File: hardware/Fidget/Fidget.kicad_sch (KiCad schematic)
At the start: 41 parts

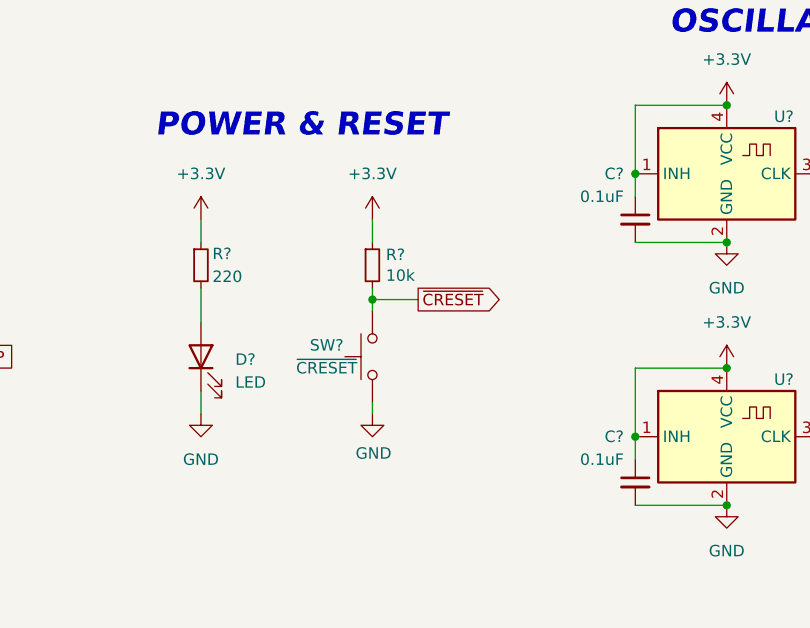
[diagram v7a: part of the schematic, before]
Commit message: Got simple RTL experiment of USART<->Bus in TinyFPGA
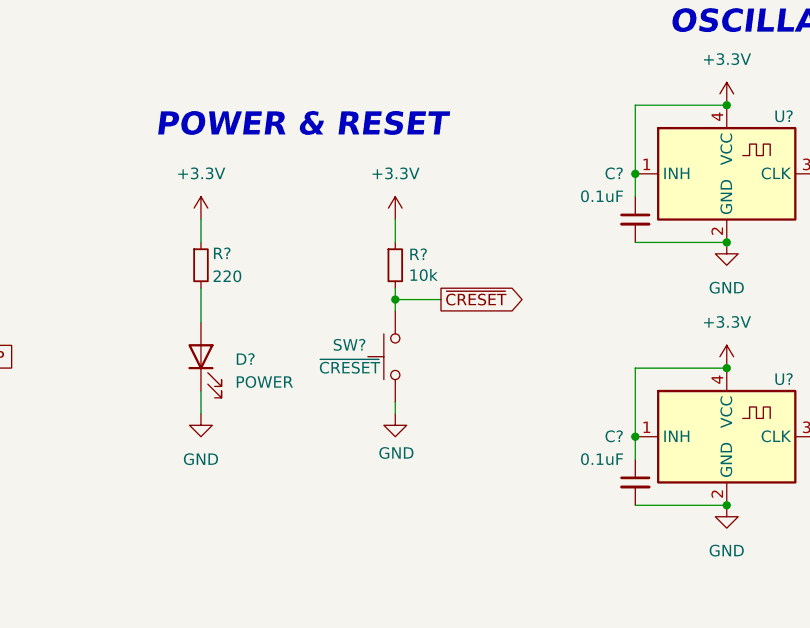
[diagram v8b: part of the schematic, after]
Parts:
- D?: value LED -> POWER
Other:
- moved on the sheet: R?, SW?
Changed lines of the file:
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@@
   (junction (at 245.11 110.49) (diameter 0) (color 0 0 0 0)
   )
-  (junction (at 205.74 132.08) (diameter 0) (color 0 0 0 0)
+  (junction (at 208.28 132.08) (diameter 0) (color 0 0 0 0)
   )
   (junction (at 110.49 130.81) (diameter 0) (color 0 0 0 0)
@@
     (stroke (width 0) (type default) (color 0 0 0 0))
   )
-  (wire (pts (xy 210.82 132.08) (xy 205.74 132.08))
-    (stroke (width 0) (type default) (color 0 0 0 0))
-  )
-  (wire (pts (xy 205.74 132.08) (xy 205.74 130.81))
+  (wire (pts (xy 213.36 132.08) (xy 208.28 132.08))
+    (stroke (width 0) (type default) (color 0 0 0 0))
+  )
+  (wire (pts (xy 208.28 132.08) (xy 208.28 130.81))
     (stroke (width 0) (type default) (color 0 0 0 0))
   )
@@
     (stroke (width 0) (type default) (color 0 0 0 0))
   )
-  (wire (pts (xy 205.74 123.19) (xy 205.74 125.73))
+  (wire (pts (xy 208.28 123.19) (xy 208.28 125.73))
     (stroke (width 0) (type default) (color 0 0 0 0))
   )
@@
     (stroke (width 0) (type default) (color 0 0 0 0))
   )
-  (wire (pts (xy 205.74 132.08) (xy 205.74 133.35))
+  (wire (pts (xy 208.28 132.08) (xy 208.28 133.35))
     (stroke (width 0) (type default) (color 0 0 0 0))
   )
@@
     (stroke (width 0) (type default) (color 0 0 0 0))
   )
-  (wire (pts (xy 205.74 143.51) (xy 205.74 144.78))
+  (wire (pts (xy 208.28 143.51) (xy 208.28 144.78))
     (stroke (width 0) (type default) (color 0 0 0 0))
   )
@@
     )
   )
-  (global_label "~{CRESET}" (shape output) (at 210.82 132.08 0) (fields_autoplaced)
+  (global_label "~{CRESET}" (shape output) (at 213.36 132.08 0) (fields_autoplaced)
     (effects (font (size 1.27 1.27)) (justify left))
-    (property "Intersheet References" "${INTERSHEET_REFS}" (id 0) (at 220.2483 132.0006 0)
+    (property "Intersheet References" "${INTERSHEET_REFS}" (id 0) (at 222.7883 132.0006 0)
       (effects (font (size 1.27 1.27)) (justify left) hide)
     )
@@
     (pin "1")
   )
-  (symbol (lib_id "Device:R_Small") (at 205.74 128.27 0) (unit 1)
-    (in_bom yes) (on_board yes)
-    (property "Reference" "R?" (id 0) (at 207.2386 127.1016 0)
-      (effects (font (size 1.27 1.27)) (justify left))
-    )
-    (property "Value" "10k" (id 1) (at 207.2386 129.413 0)
-      (effects (font (size 1.27 1.27)) (justify left))
-    )
-    (property "Footprint" "Resistor_THT:R_Axial_DIN0204_L3.6mm_D1.6mm_P5.08mm_Horizontal" (id 2) (at 205.74 128.27 0)
-      (effects (font (size 1.27 1.27)) hide)
-    )
-    (property "Datasheet" "~" (id 3) (at 205.74 128.27 0)
+  (symbol (lib_id "Device:R_Small") (at 208.28 128.27 0) (unit 1)
+    (in_bom yes) (on_board yes)
+    (property "Reference" "R?" (id 0) (at 209.7786 127.1016 0)
+      (effects (font (size 1.27 1.27)) (justify left))
+    )
+    (property "Value" "10k" (id 1) (at 209.7786 129.413 0)
+      (effects (font (size 1.27 1.27)) (justify left))
+    )
+    (property "Footprint" "Resistor_THT:R_Axial_DIN0204_L3.6mm_D1.6mm_P5.08mm_Horizontal" (id 2) (at 208.28 128.27 0)
+      (effects (font (size 1.27 1.27)) hide)
+    )
+    (property "Datasheet" "~" (id 3) (at 208.28 128.27 0)
       (effects (font (size 1.27 1.27)) hide)
     )
@@
     (pin "1")
   )
-  (symbol (lib_id "power:+3.3V") (at 205.74 123.19 0) (unit 1)
-    (in_bom yes) (on_board yes) (fields_autoplaced)
-    (property "Reference" "#PWR0149" (id 0) (at 205.74 127 0)
-      (effects (font (size 1.27 1.27)) hide)
-    )
-    (property "Value" "+3.3V" (id 1) (at 205.74 118.11 0))
-    (property "Footprint" "" (id 2) (at 205.74 123.19 0)
-      (effects (font (size 1.27 1.27)) hide)
-    )
-    (property "Datasheet" "" (id 3) (at 205.74 123.19 0)
+  (symbol (lib_id "power:+3.3V") (at 208.28 123.19 0) (unit 1)
+    (in_bom yes) (on_board yes) (fields_autoplaced)
+    (property "Reference" "#PWR0149" (id 0) (at 208.28 127 0)
+      (effects (font (size 1.27 1.27)) hide)
+    )
+    (property "Value" "+3.3V" (id 1) (at 208.28 118.11 0))
+    (property "Footprint" "" (id 2) (at 208.28 123.19 0)
+      (effects (font (size 1.27 1.27)) hide)
+    )
+    (property "Datasheet" "" (id 3) (at 208.28 123.19 0)
       (effects (font (size 1.27 1.27)) hide)
     )
@@
     (pin "2")
   )
-  (symbol (lib_id "power:GND") (at 205.74 144.78 0) (unit 1)
-    (in_bom yes) (on_board yes)
-    (property "Reference" "#PWR0150" (id 0) (at 205.74 151.13 0)
-      (effects (font (size 1.27 1.27)) hide)
-    )
-    (property "Value" "GND" (id 1) (at 205.867 149.1742 0))
-    (property "Footprint" "" (id 2) (at 205.74 144.78 0)
-      (effects (font (size 1.27 1.27)) hide)
-    )
-    (property "Datasheet" "" (id 3) (at 205.74 144.78 0)
+  (symbol (lib_id "power:GND") (at 208.28 144.78 0) (unit 1)
+    (in_bom yes) (on_board yes)
+    (property "Reference" "#PWR0150" (id 0) (at 208.28 151.13 0)
+      (effects (font (size 1.27 1.27)) hide)
+    )
+    (property "Value" "GND" (id 1) (at 208.407 149.1742 0))
+    (property "Footprint" "" (id 2) (at 208.28 144.78 0)
+      (effects (font (size 1.27 1.27)) hide)
+    )
+    (property "Datasheet" "" (id 3) (at 208.28 144.78 0)
       (effects (font (size 1.27 1.27)) hide)
     )
@@
     (pin "2")
   )
-  (symbol (lib_id "Switch:SW_Push") (at 205.74 138.43 90) (unit 1)
-    (in_bom yes) (on_board yes)
-    (property "Reference" "SW?" (id 0) (at 200.66 137.16 90))
-    (property "Value" "~{CRESET}" (id 1) (at 200.66 139.7 90))
-    (property "Footprint" "Button_Switch_THT:SW_PUSH_6mm" (id 2) (at 200.66 138.43 0)
-      (effects (font (size 1.27 1.27)) hide)
-    )
-    (property "Datasheet" "~" (id 3) (at 200.66 138.43 0)
+  (symbol (lib_id "Switch:SW_Push") (at 208.28 138.43 90) (unit 1)
+    (in_bom yes) (on_board yes)
+    (property "Reference" "SW?" (id 0) (at 203.2 137.16 90))
+    (property "Value" "~{CRESET}" (id 1) (at 203.2 139.7 90))
+    (property "Footprint" "Button_Switch_THT:SW_PUSH_6mm" (id 2) (at 203.2 138.43 0)
+      (effects (font (size 1.27 1.27)) hide)
+    )
+    (property "Datasheet" "~" (id 3) (at 203.2 138.43 0)
       (effects (font (size 1.27 1.27)) hide)
     )
@@
       (effects (font (size 1.27 1.27)) (justify right))
     )
-    (property "Value" "LED" (id 1) (at 190.5 141.2874 90)
+    (property "Value" "POWER" (id 1) (at 190.5 141.2874 90)
       (effects (font (size 1.27 1.27)) (justify right))
     )
@@
       (reference "#PWR0201") (unit 1) (value "+3.3V") (footprint "")
     )
+    (path "/78dabe45-a56e-4c1c-abf8-a53679340cd9/32af5117-4867-459b-9fc5-3930d31b079c"
+      (reference "#PWR?") (unit 1) (value "GND") (footprint "")
+    )
+    (path "/78dabe45-a56e-4c1c-abf8-a53679340cd9/4a6908bb-cf20-4883-990b-62288f60f364"
+      (reference "#PWR?") (unit 1) (value "GND") (footprint "")
+    )
+    (path "/78dabe45-a56e-4c1c-abf8-a53679340cd9/5ad1548b-6500-4e21-9929-dc51aff281a5"
+      (reference "#PWR?") (unit 1) (value "+3.3V") (footprint "")
+    )
+    (path "/78dabe45-a56e-4c1c-abf8-a53679340cd9/646e8379-3038-4153-ab95-dc981463368d"
+      (reference "#PWR?") (unit 1) (value "GND") (footprint "")
+    )
+    (path "/78dabe45-a56e-4c1c-abf8-a53679340cd9/712d8644-5eb7-4bcc-bfe9-8b7f5c84fca8"
+      (reference "#PWR?") (unit 1) (value "+3.3V") (footprint "")
+    )
+    (path "/78dabe45-a56e-4c1c-abf8-a53679340cd9/b5d5925b-ed9f-4e3a-b427-99111acc3c01"
+      (reference "#PWR?") (unit 1) (value "GND") (footprint "")
+    )
     (path "/636ee855-2082-46e2-a822-b2da99283a14/0104126c-d7db-4e9c-879f-fe393c49bd40"
       (reference "C?") (unit 1) (value "0.1uF") (footprint "")
@@
       (reference "C?") (unit 1) (value "0.1uF") (footprint "")
     )
+    (path "/78dabe45-a56e-4c1c-abf8-a53679340cd9/2ee9b547-73b8-4502-8eb1-38d06f282605"
+      (reference "D?") (unit 1) (value "UL1") (footprint "")
+    )
+    (path "/78dabe45-a56e-4c1c-abf8-a53679340cd9/929e1288-08e9-45d3-95e0-6f0f74cf978f"
+      (reference "D?") (unit 1) (value "UL2") (footprint "")
+    )
     (path "/fc064560-d1a5-4c2f-a4ad-ae42d5f9cadb"
-      (reference "D?") (unit 1) (value "LED") (footprint "")
+      (reference "D?") (unit 1) (value "POWER") (footprint "")
     )
     (path "/02f7746c-715c-4734-bcc3-9f6f4cf1447e"
@@
       (reference "R?") (unit 1) (value "68") (footprint "")
     )
+    (path "/78dabe45-a56e-4c1c-abf8-a53679340cd9/19d67f88-a082-4c8d-8f95-07e071cfad85"
+      (reference "R?") (unit 1) (value "10k") (footprint "Resistor_THT:R_Axial_DIN0204_L3.6mm_D1.6mm_P5.08mm_Horizontal")
+    )
+    (path "/78dabe45-a56e-4c1c-abf8-a53679340cd9/1f10bb6d-c48a-4e92-82ff-956ea432e3c4"
+      (reference "R?") (unit 1) (value "220") (footprint "")
+    )
     (path "/246cd007-a62a-4320-a6c2-e9412f150d57"
       (reference "R?") (unit 1) (value "10k") (footprint "Resistor_THT:R_Axial_DIN0204_L3.6mm_D1.6mm_P5.08mm_Horizontal")
@@
       (reference "R?") (unit 1) (value "10k") (footprint "")
     )
+    (path "/78dabe45-a56e-4c1c-abf8-a53679340cd9/4e1559ce-f53d-4a0a-82b9-1e3c385e7fd5"
+      (reference "R?") (unit 1) (value "220") (footprint "")
+    )
     (path "/58e0c44d-16dc-4202-8a03-b6498121ec3e"
       (reference "R?") (unit 1) (value "220") (footprint "")
@@
       (reference "R?") (unit 1) (value "100") (footprint "")
     )
+    (path "/78dabe45-a56e-4c1c-abf8-a53679340cd9/a977fb27-e139-458f-9717-f139a12bc595"
+      (reference "R?") (unit 1) (value "10k") (footprint "Resistor_THT:R_Axial_DIN0204_L3.6mm_D1.6mm_P5.08mm_Horizontal")
+    )
     (path "/aa843138-0bf5-4d08-a1a1-806febcbb8b6"
       (reference "R?") (unit 1) (value "68") (footprint "")
@@
       (reference "R?") (unit 1) (value "10k") (footprint "")
     )
+    (path "/78dabe45-a56e-4c1c-abf8-a53679340cd9/6e55659e-d6c8-4170-9113-80c63dcaa738"
+      (reference "SW?") (unit 1) (value "UB1") (footprint "Button_Switch_THT:SW_PUSH_6mm")
+    )
+    (path "/78dabe45-a56e-4c1c-abf8-a53679340cd9/b050c58f-3821-4d73-ba2a-1b8d7fad9012"
+      (reference "SW?") (unit 1) (value "UB1") (footprint "Button_Switch_THT:SW_PUSH_6mm")
+    )
     (path "/ca0acf94-c6e7-4ef9-9d99-3b7348ef6d00"
